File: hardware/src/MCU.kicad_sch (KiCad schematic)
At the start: 19 parts, among them SW201 SW_Push, SW202 SW_Push, U201 ESP32-C3-WROOM-02, U202 TLV1117LV33

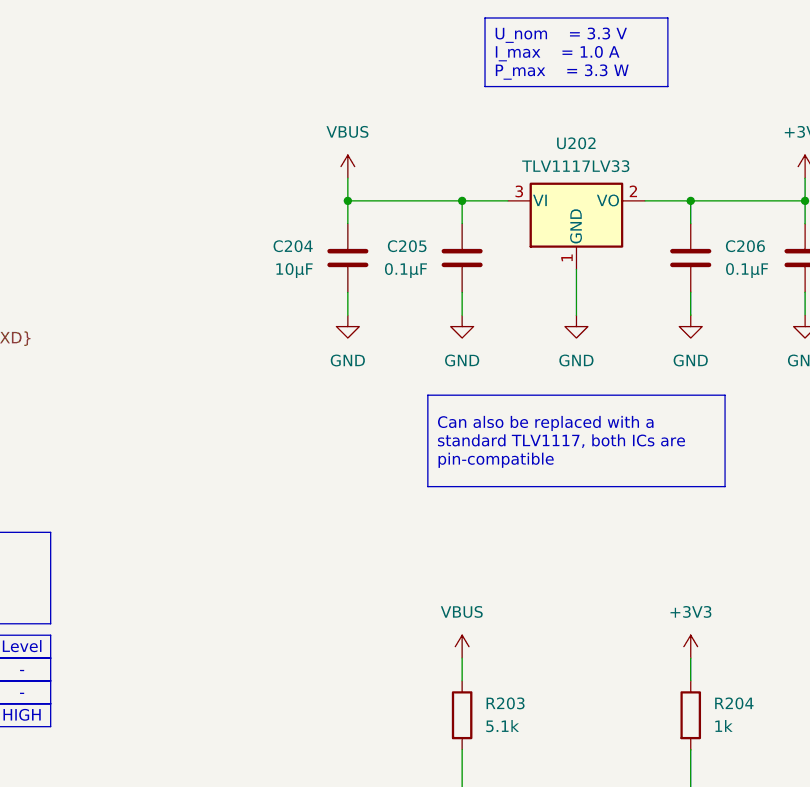
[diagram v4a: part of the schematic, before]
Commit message: Add: Level Shifter +3V3 to +5V
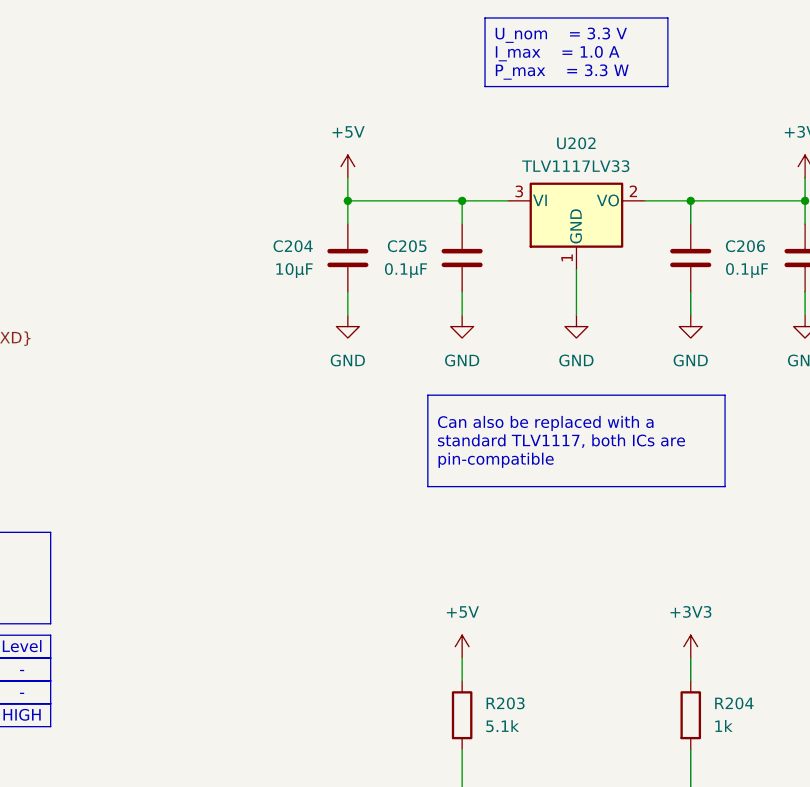
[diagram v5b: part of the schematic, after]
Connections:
- net VBUS renamed +5V
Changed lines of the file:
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@@
+	)
+	(symbol
+		(lib_id "power:+5V")
+		(at 190.5 60.96 0)
+		(unit 1)
+		(exclude_from_sim no)
+		(in_bom yes)
+		(on_board yes)
+		(dnp no)
+		(fields_autoplaced yes)
+		(property "Reference" "#PWR0210"
+			(at 190.5 64.77 0)
+			(effects
+				(font
+					(size 1.27 1.27)
+				)
+				(hide yes)
+			)
+		)
+		(property "Value" "+5V"
+			(at 190.5 55.88 0)
+			(effects
+				(font
+					(size 1.27 1.27)
+				)
+			)
+		)
+		(property "Footprint" ""
+			(at 190.5 60.96 0)
+			(effects
+				(font
+					(size 1.27 1.27)
+				)
+				(hide yes)
+			)
+		)
+		(property "Datasheet" ""
+			(at 190.5 60.96 0)
+			(effects
+				(font
+					(size 1.27 1.27)
+				)
+				(hide yes)
+			)
+		)
+		(property "Description" "Power symbol creates a global label with name \"+5V\""
+			(at 190.5 60.96 0)
+			(effects
+				(font
+					(size 1.27 1.27)
+				)
+				(hide yes)
+			)
+		)
+		(pin "1"
+		)
+		(instances
+			(project "ESP-Wordclock"
+				(path "/bfaac094-0365-40a4-8b7a-d4d62ace544e/148425c6-8949-47fb-990d-0e511c74cf4c"
+					(reference "#PWR0210")
+					(unit 1)
+				)
+			)
+		)
 	)
 	(symbol
@@
 	)
 	(symbol
+		(lib_id "power:+5V")
+		(at 203.2 114.3 0)
+		(unit 1)
+		(exclude_from_sim no)
+		(in_bom yes)
+		(on_board yes)
+		(dnp no)
+		(fields_autoplaced yes)
+		(property "Reference" "#PWR0213"
+			(at 203.2 118.11 0)
+			(effects
+				(font
+					(size 1.27 1.27)
+				)
+				(hide yes)
+			)
+		)
+		(property "Value" "+5V"
+			(at 203.2 109.22 0)
+			(effects
+				(font
+					(size 1.27 1.27)
+				)
+			)
+		)
+		(property "Footprint" ""
+			(at 203.2 114.3 0)
+			(effects
+				(font
+					(size 1.27 1.27)
+				)
+				(hide yes)
+			)
+		)
+		(property "Datasheet" ""
+			(at 203.2 114.3 0)
+			(effects
+				(font
+					(size 1.27 1.27)
+				)
+				(hide yes)
+			)
+		)
+		(property "Description" "Power symbol creates a global label with name \"+5V\""
+			(at 203.2 114.3 0)
+			(effects
+				(font
+					(size 1.27 1.27)
+				)
+				(hide yes)
+			)
+		)
+		(pin "1"
+		)
+		(instances
+			(project ""
+				(path "/bfaac094-0365-40a4-8b7a-d4d62ace544e/148425c6-8949-47fb-990d-0e511c74cf4c"
+					(reference "#PWR0213")
+					(unit 1)
+				)
+			)
+		)
+	)
+	(symbol
 		(lib_id "Device:LED")
 		(at 203.2 133.35 90)
@@
 				(path "/bfaac094-0365-40a4-8b7a-d4d62ace544e/148425c6-8949-47fb-990d-0e511c74cf4c"
 					(reference "D202")
-					(unit 1)
-				)
-			)
-		)
-	)
-	(symbol
-		(lib_id "power:VBUS")
-		(at 190.5 60.96 0)
-		(unit 1)
-		(exclude_from_sim no)
-		(in_bom yes)
-		(on_board yes)
-		(dnp no)
-		(fields_autoplaced yes)
-		(property "Reference" "#PWR0210"
-			(at 190.5 64.77 0)
-			(effects
-				(font
-					(size 1.27 1.27)
-				)
-				(hide yes)
-			)
-		)
-		(property "Value" "VBUS"
-			(at 190.5 55.88 0)
-			(effects
-				(font
-					(size 1.27 1.27)
-				)
-			)
-		)
-		(property "Footprint" ""
-			(at 190.5 60.96 0)
-			(effects
-				(font
-					(size 1.27 1.27)
-				)
-				(hide yes)
-			)
-		)
-		(property "Datasheet" ""
-			(at 190.5 60.96 0)
-			(effects
-				(font
-					(size 1.27 1.27)
-				)
-				(hide yes)
-			)
-		)
-		(property "Description" "Power symbol creates a global label with name \"VBUS\""
-			(at 190.5 60.96 0)
-			(effects
-				(font
-					(size 1.27 1.27)
-				)
-				(hide yes)
-			)
-		)
-		(pin "1"
-		)
-		(instances
-			(project ""
-				(path "/bfaac094-0365-40a4-8b7a-d4d62ace544e/148425c6-8949-47fb-990d-0e511c74cf4c"
-					(reference "#PWR0210")
 					(unit 1)
 				)
@@
 					(unit 1)
 				)
-			)
-		)
-	)
-	(symbol
-		(lib_id "power:VBUS")
-		(at 203.2 114.3 0)
-		(unit 1)
-		(exclude_from_sim no)
-		(in_bom yes)
-		(on_board yes)
-		(dnp no)
-		(fields_autoplaced yes)
-		(property "Reference" "#PWR0213"
-			(at 203.2 118.11 0)
-			(effects
-				(font
-					(size 1.27 1.27)
-				)
-				(hide yes)
-			)
-		)
-		(property "Value" "VBUS"
-			(at 203.2 109.22 0)
-			(effects
-				(font
-					(size 1.27 1.27)
-				)
-			)
-		)
-		(property "Footprint" ""
-			(at 203.2 114.3 0)
-			(effects
-				(font
-					(size 1.27 1.27)
-				)
-				(hide yes)
-			)
-		)
-		(property "Datasheet" ""
-			(at 203.2 114.3 0)
-			(effects
-				(font
-					(size 1.27 1.27)
-				)
-				(hide yes)
-			)
-		)
-		(property "Description" "Power symbol creates a global label with name \"VBUS\""
-			(at 203.2 114.3 0)
-			(effects
-				(font
-					(size 1.27 1.27)
-				)
-				(hide yes)
-			)
-		)
-		(pin "1"
-		)
-		(instances
-			(project "ESP-Wordclock"
-				(path "/bfaac094-0365-40a4-8b7a-d4d62ace544e/148425c6-8949-47fb-990d-0e511c74cf4c"
-					(reference "#PWR0213")
-					(unit 1)
-				)

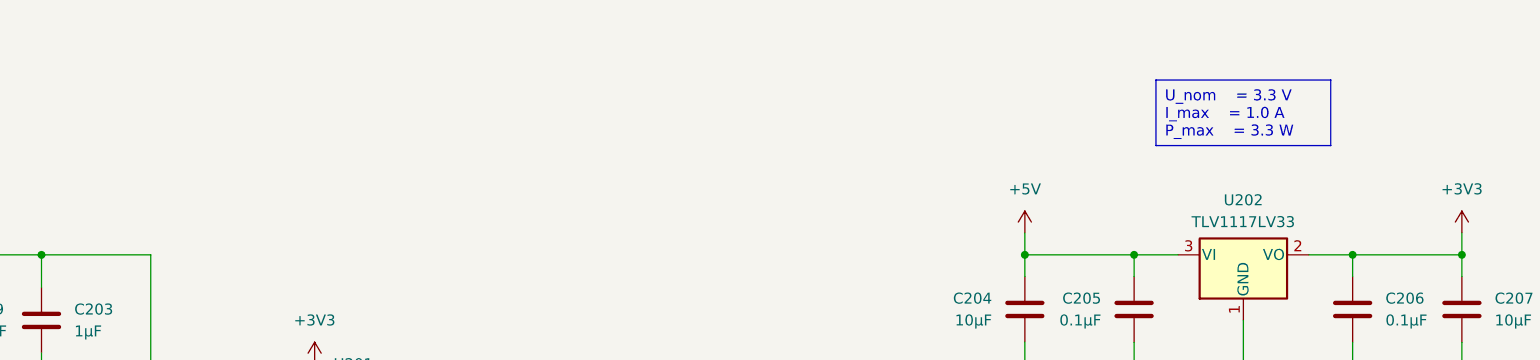
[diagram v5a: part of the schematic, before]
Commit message: Add: Text Headers to the indidual schematic regions
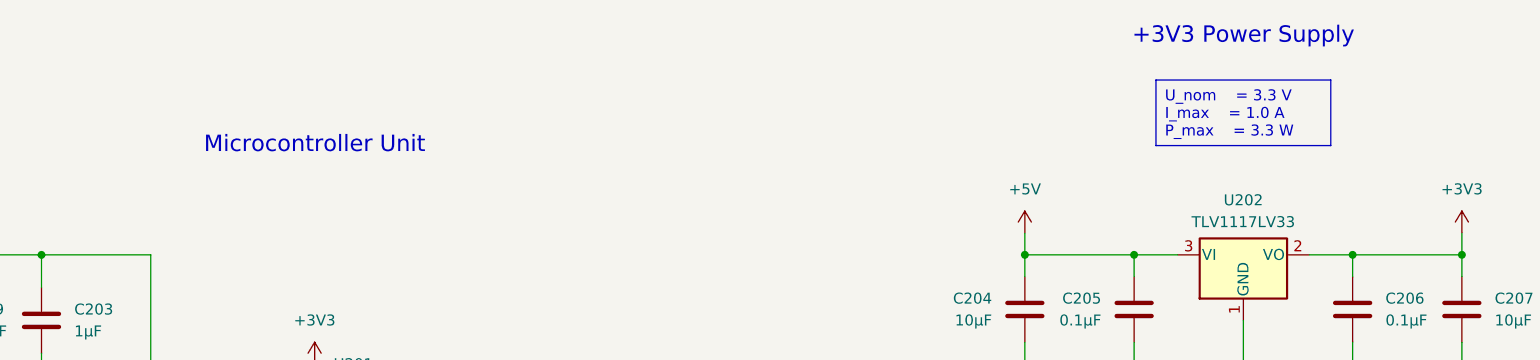
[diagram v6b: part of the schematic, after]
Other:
- note added: "+3V3 Power Supply"
- note added: "Microcontroller Unit"
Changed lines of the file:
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@@
+		)
+	)
+	(text "+3V3 Power Supply"
+		(exclude_from_sim no)
+		(at 215.9 38.1 0)
+		(effects
+			(font
+				(size 1.905 1.905)
+			)
+		)
+	)
+	(text "Microcontroller Unit"
+		(exclude_from_sim no)
+		(at 107.95 50.8 0)
+		(effects
+			(font
+				(size 1.905 1.905)
+			)
 		)
 	)

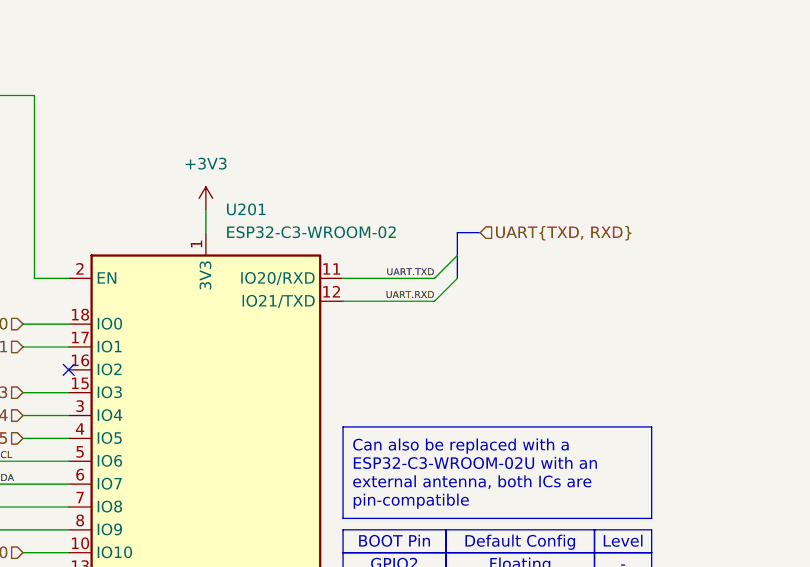
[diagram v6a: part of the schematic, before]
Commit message: Mod: UART, changed position where the TXD and RXD are switched
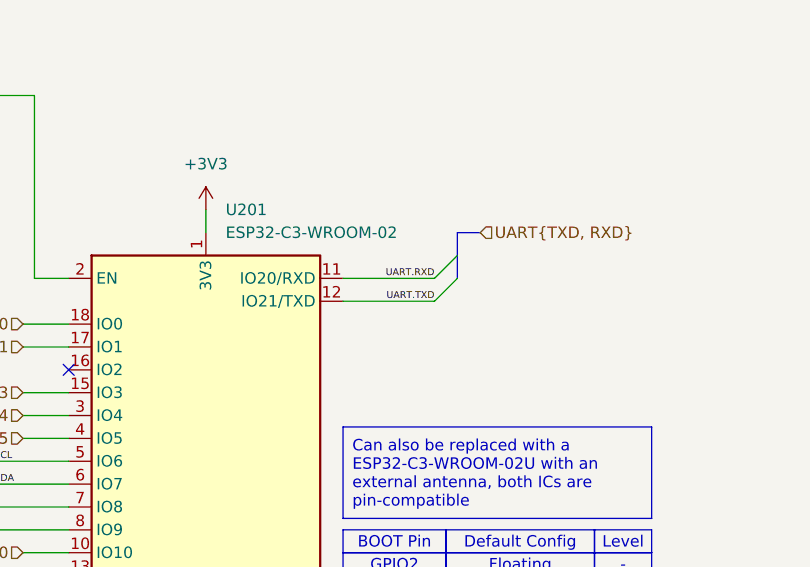
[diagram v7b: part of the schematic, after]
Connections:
- net UART.RXD: now also U201.11 (IO20/RXD); no longer U201.12 (IO21/TXD)
- net UART.TXD: now also U201.12 (IO21/TXD); no longer U201.11 (IO20/RXD)
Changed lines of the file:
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@@
 	)
 	(label "UART.RXD"
-		(at 133.35 86.36 180)
+		(at 133.35 83.82 180)
 		(fields_autoplaced yes)
 		(effects
@@
 	)
 	(label "UART.TXD"
-		(at 133.35 83.82 180)
+		(at 133.35 86.36 180)
 		(fields_autoplaced yes)
 		(effects
